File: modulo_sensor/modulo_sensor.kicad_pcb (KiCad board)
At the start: 2 copper layers, 112.4 x 36.6 mm, 33 parts, among them J1 Conn_01x08_Pin, U1 74HC14DR2G

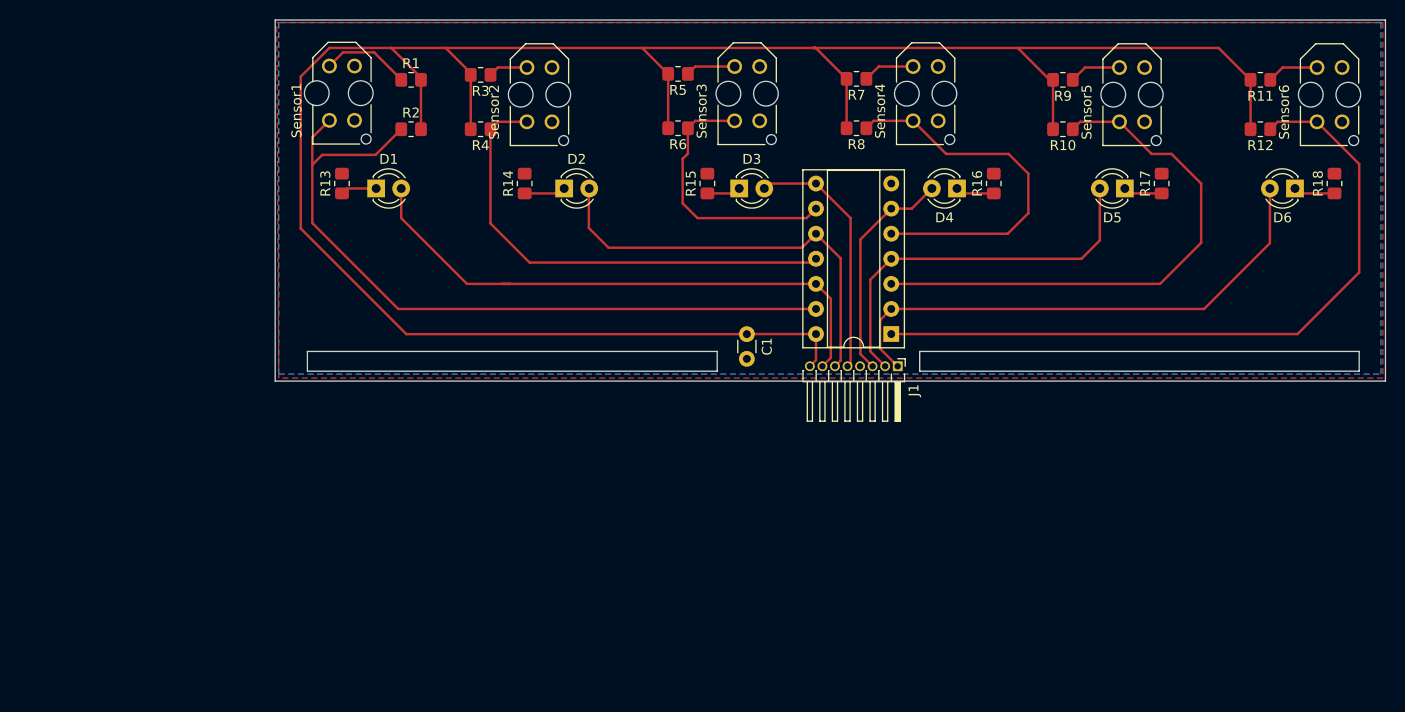
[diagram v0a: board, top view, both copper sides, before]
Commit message: refactor: Pongo el integrado en horizontal
Está todo conectado como antes
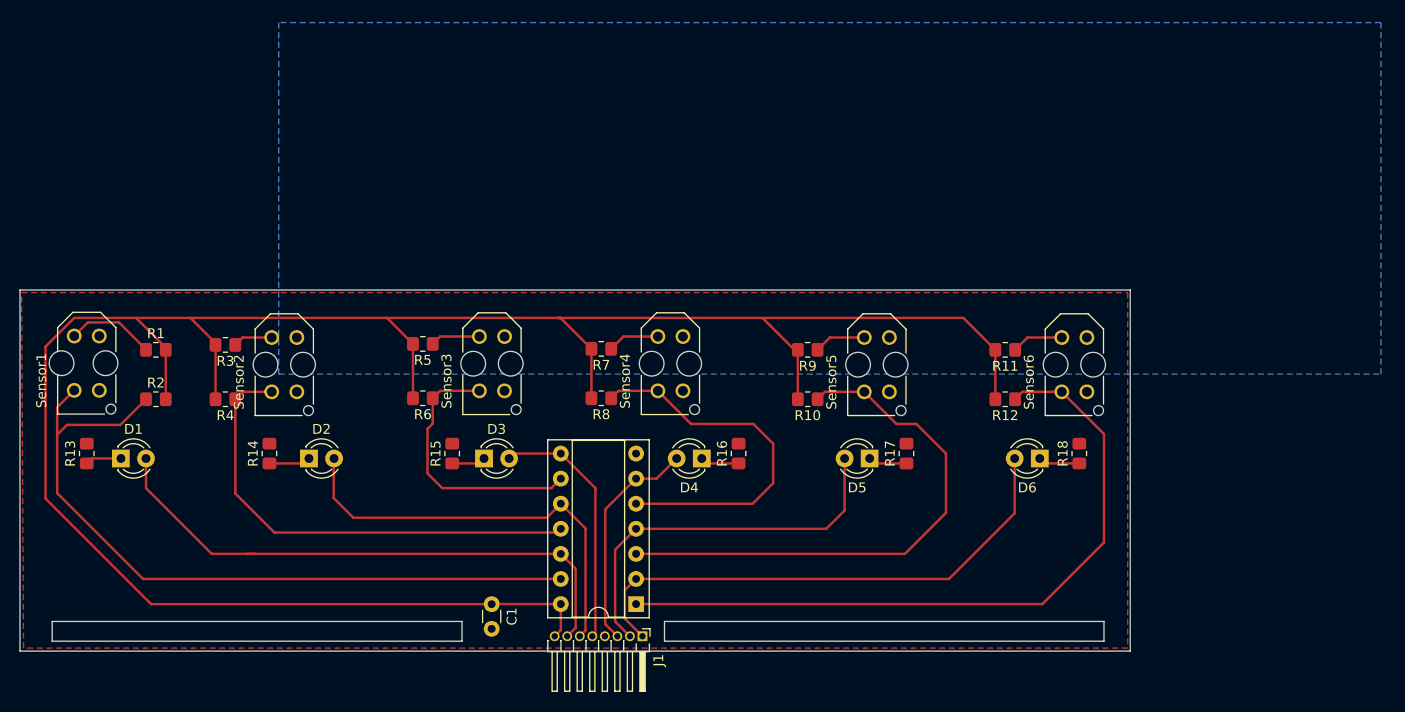
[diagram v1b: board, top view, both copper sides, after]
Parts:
- moved C1 37.6 mm to (90.2, 87.1)
- moved D2 37.6 mm to (71.7, 72.3)
- moved D4 37.6 mm to (111.4, 72.3)
- moved D5 37.6 mm to (128.4, 72.3)
- moved D6 37.6 mm to (145.7, 72.3)
- moved J1 37.6 mm to (105.4, 90.3)
- moved R1 37.6 mm to (56.2, 61.3)
- moved R10 37.6 mm to (122.2, 66.3)
- moved R11 37.6 mm to (142.2, 61.3)
- moved R12 37.6 mm to (142.2, 66.3)
- moved R13 37.6 mm to (49.2, 71.8)
- moved R14 37.6 mm to (67.7, 71.8)
- moved R15 37.6 mm to (86.2, 71.8)
- moved R16 37.6 mm to (115.2, 71.8)
- moved R17 37.6 mm to (132.2, 71.8)
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
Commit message: fix: Guardo el archivo (fallo del commit anterior)
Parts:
- moved U1 13.8 mm to (94.9, 77.4), turned to -90 degrees
- moved D4 5.27 mm to (106.5, 70.5)
- moved R16 4.67 mm to (110.5, 71.5), turned to -90 degrees
- moved C1 2.43 mm to (92.5, 87.8)
- moved D5 2.31 mm to (127.0, 70.5)
- moved R17 2.19 mm to (130.0, 71.5), turned to -90 degrees
- moved D1 1.84 mm to (52.6, 70.5)
- moved D2 1.84 mm to (71.7, 70.5)
- moved D3 1.84 mm to (89.4, 70.5)
- moved D6 1.84 mm to (145.7, 70.5)
- moved J1 1.61 mm to (104.8, 88.8)
- moved R1 0.84 mm to (56.2, 60.5)
- moved R11 0.84 mm to (142.2, 60.5)
- moved R9 0.84 mm to (122.2, 60.5)
- moved R7 0.74 mm to (101.3, 60.5)
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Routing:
- net /Led_Sensor4: track 22.7 -> 52.8 mm
- net /Led_Sensor3: track 25.5 -> 54.6 mm
- net GND: track 0.62 -> 28.0 mm
- net /Led_Sensor5: track 39.5 -> 63.7 mm
- net /Sensor6: track 72.1 -> 57.9 mm
- net /Led_Sensor6: track 53.6 -> 67.7 mm
- net vcc: track 227.2 -> 239.4 mm
- net /Sensor3: track 27.4 -> 37.3 mm
- net /Sensor4: track 37.7 -> 46.7 mm
- net /Led_Sensor2: track 43.2 -> 48.9 mm
- net /Sensor5: track 55.0 -> 59.3 mm
- net /Sensor2: track 48.3 -> 52.3 mm
- net /Led_Sensor1: track 57.9 -> 60.9 mm
- net /Sensor1: track 76.2 -> 73.4 mm
- net Net-(D5-K): track 3.93 -> 2.96 mm
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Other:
- outline, holes or cut-outs redrawn

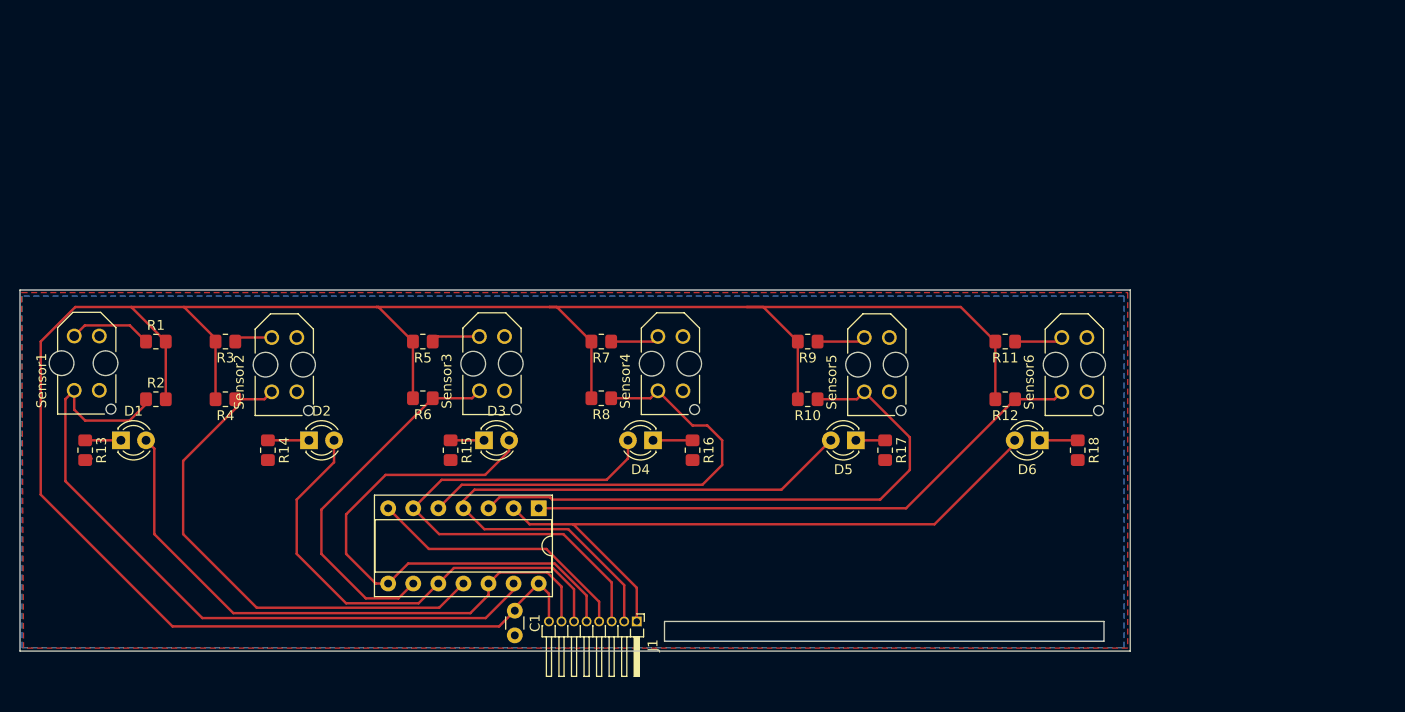
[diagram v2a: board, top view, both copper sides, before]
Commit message: refactor: Los sensores ahora están en la capa de abajo
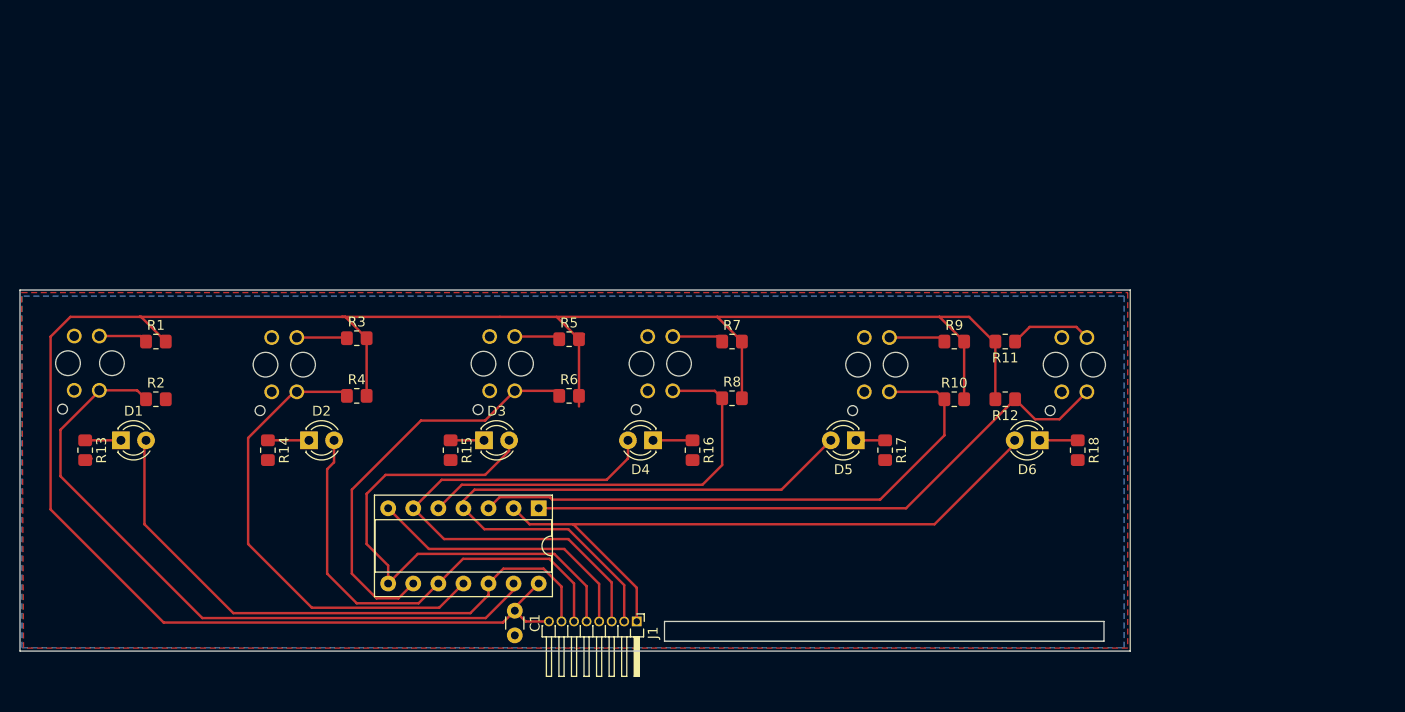
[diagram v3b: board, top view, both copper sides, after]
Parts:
- Sensor1, Sensor2, Sensor3, Sensor4, Sensor5, Sensor6: moved to B.Cu
- moved R10 14.8 mm to (137.0, 66.3), turned to 0 degrees
- moved R9 14.8 mm to (137.0, 60.5), turned to 0 degrees
- moved R5 14.8 mm to (98.0, 60.3), turned to 0 degrees
- moved R6 14.8 mm to (98.0, 66.0), turned to 0 degrees
- moved R3 13.3 mm to (76.5, 60.2), turned to 0 degrees
- moved R4 13.3 mm to (76.5, 66.0), turned to 0 degrees
- moved R7 13.2 mm to (114.5, 60.5), turned to 0 degrees
- moved R8 13.2 mm to (114.5, 66.2), turned to 0 degrees
- moved Sensor3 1.04 mm to (91.2, 62.7)
- moved Sensor4 1.03 mm to (107.2, 62.7)
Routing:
- net vcc: track 239.4 -> 223.7 mm
- net /Sensor3: track 37.3 -> 41.7 mm
- net /Sensor6: track 57.9 -> 62.1 mm
- net /Sensor4: track 46.7 -> 42.6 mm
- net /Sensor2: track 52.3 -> 48.3 mm
- net /Sensor1: track 73.4 -> 69.6 mm
- net Net-(R11-Pad1): track 4.90 -> 8.33 mm
- net Net-(R1-Pad1): track 8.39 -> 4.96 mm
- net GND: track 28.0 -> 30.2 mm
- net /Led_Sensor2: track 48.9 -> 46.8 mm
- net Net-(R3-Pad1): track 3.86 -> 5.10 mm
- net /Led_Sensor3: track 54.6 -> 53.5 mm
- net Net-(R9-Pad1): track 4.90 -> 5.74 mm

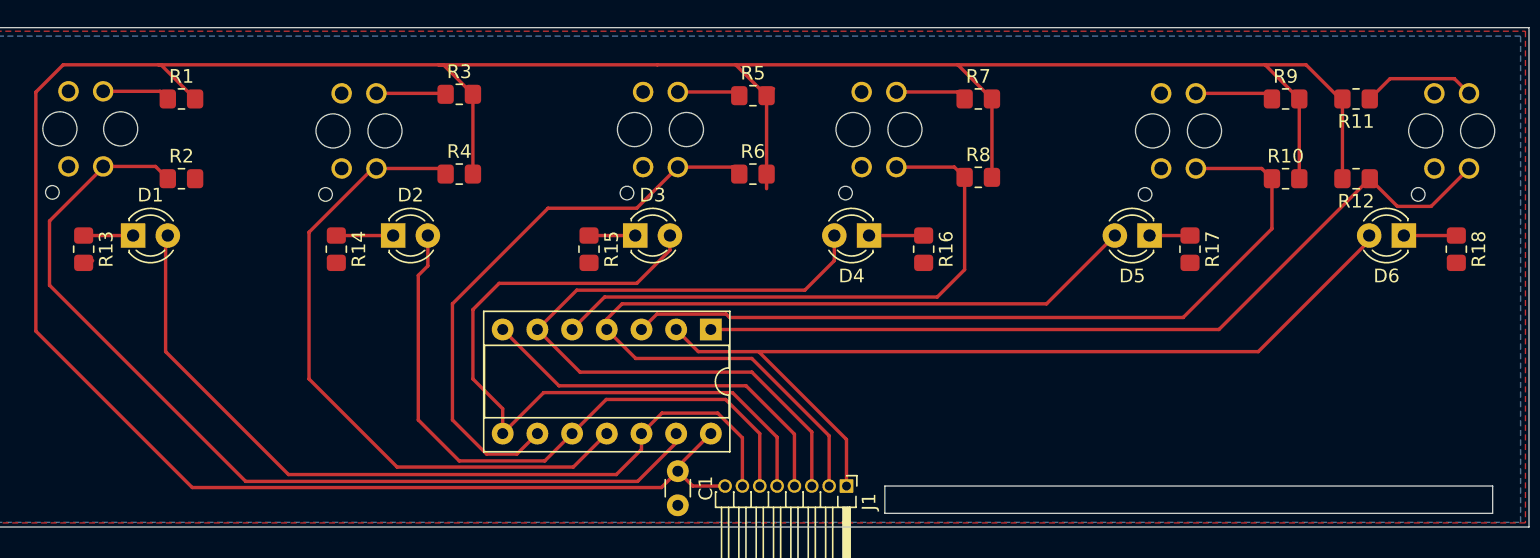
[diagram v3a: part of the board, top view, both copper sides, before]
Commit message: refactor: Cambio las huellas de los led por SMDs
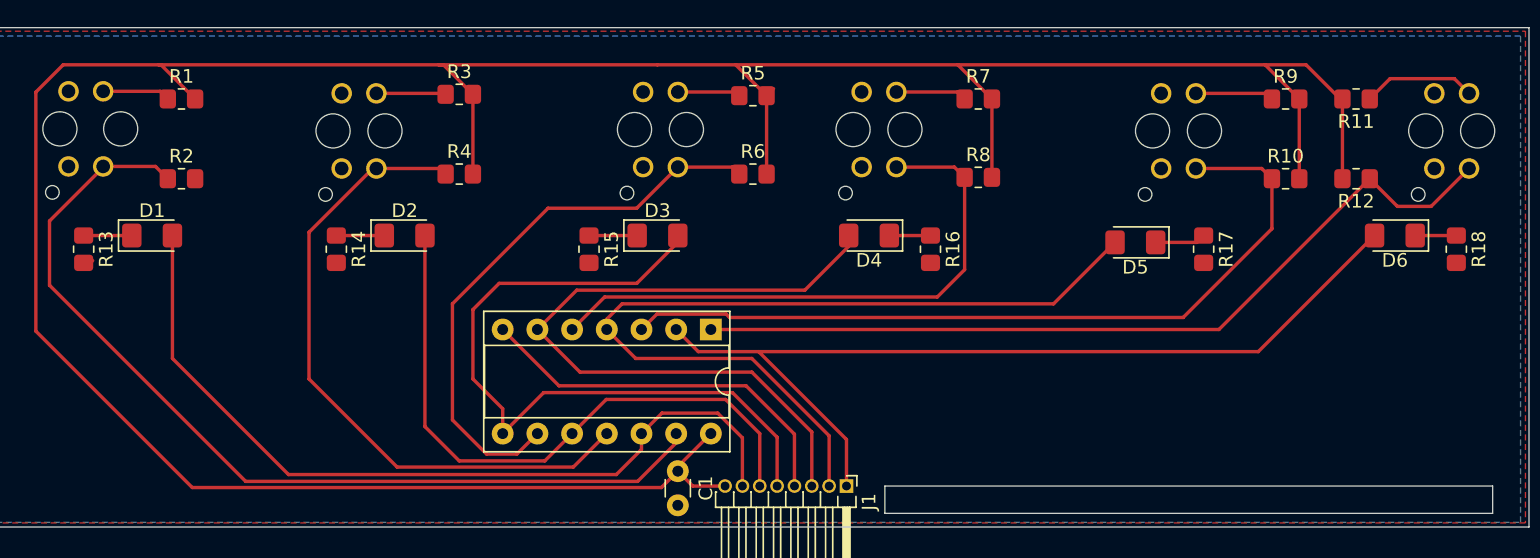
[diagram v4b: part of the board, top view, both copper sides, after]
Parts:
- D1, D2, D3, D4, D5, D6: footprint LED_THT:LED_D3.0mm -> LED_SMD:LED_1206_3216Metric_Pad1.42x1.75mm_HandSolder
- moved D3 1.63 mm to (91.0, 70.5)
- moved D1 1.39 mm to (54.0, 70.5)
- moved D5 1.15 mm to (126.0, 71.0)
- moved R17 1.00 mm to (131.0, 71.5)
- moved D2 0.84 mm to (72.5, 70.5)
- moved D6 0.66 mm to (145.0, 70.5)
- moved R16 0.50 mm to (111.0, 71.5)
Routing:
- net vcc: track 223.7 -> 222.6 mm
- net Net-(D4-K): track 4.00 -> 3.01 mm
- net Net-(D6-K): track 3.84 -> 3.01 mm
- net Net-(D5-K): track 2.96 -> 3.72 mm
- net Net-(D2-K): track 4.16 -> 3.51 mm

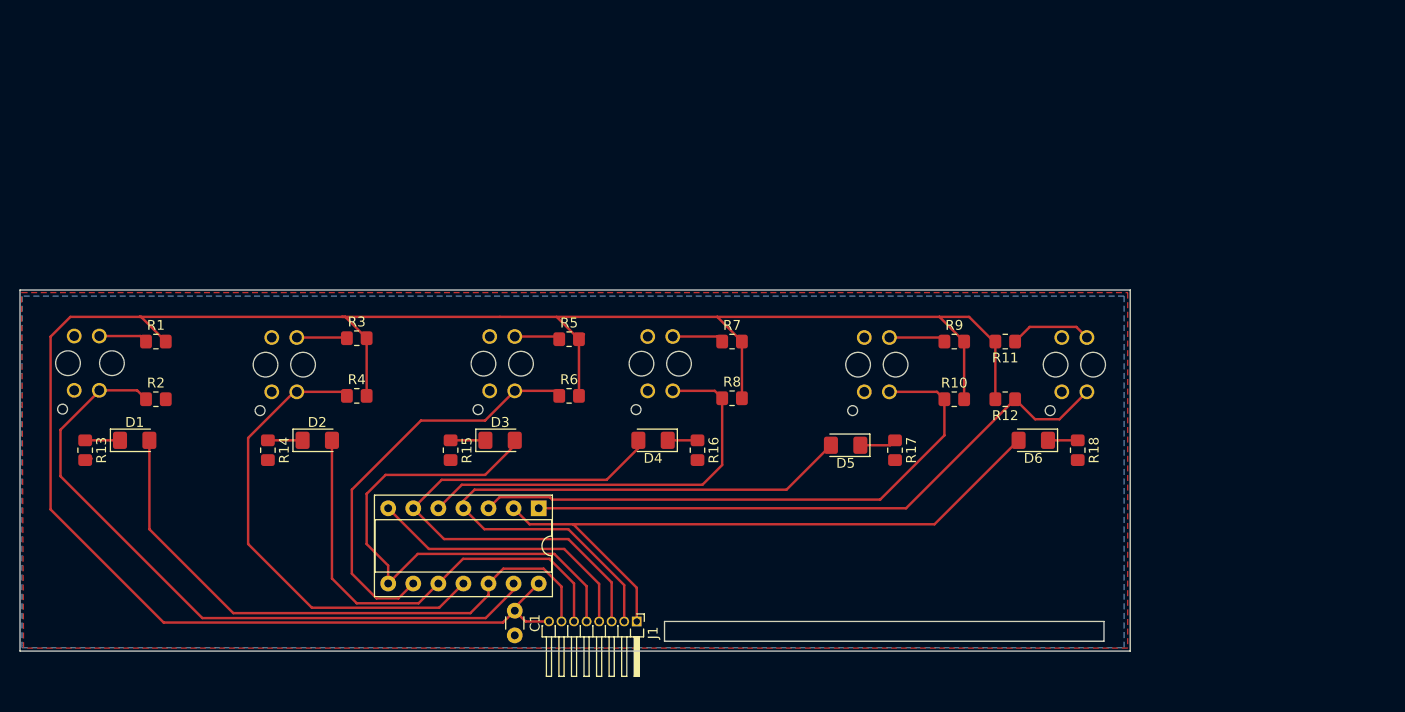
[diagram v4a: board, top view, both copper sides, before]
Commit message: feat: Reestructuro la placa a doble faz y pasa el DRC sin errores
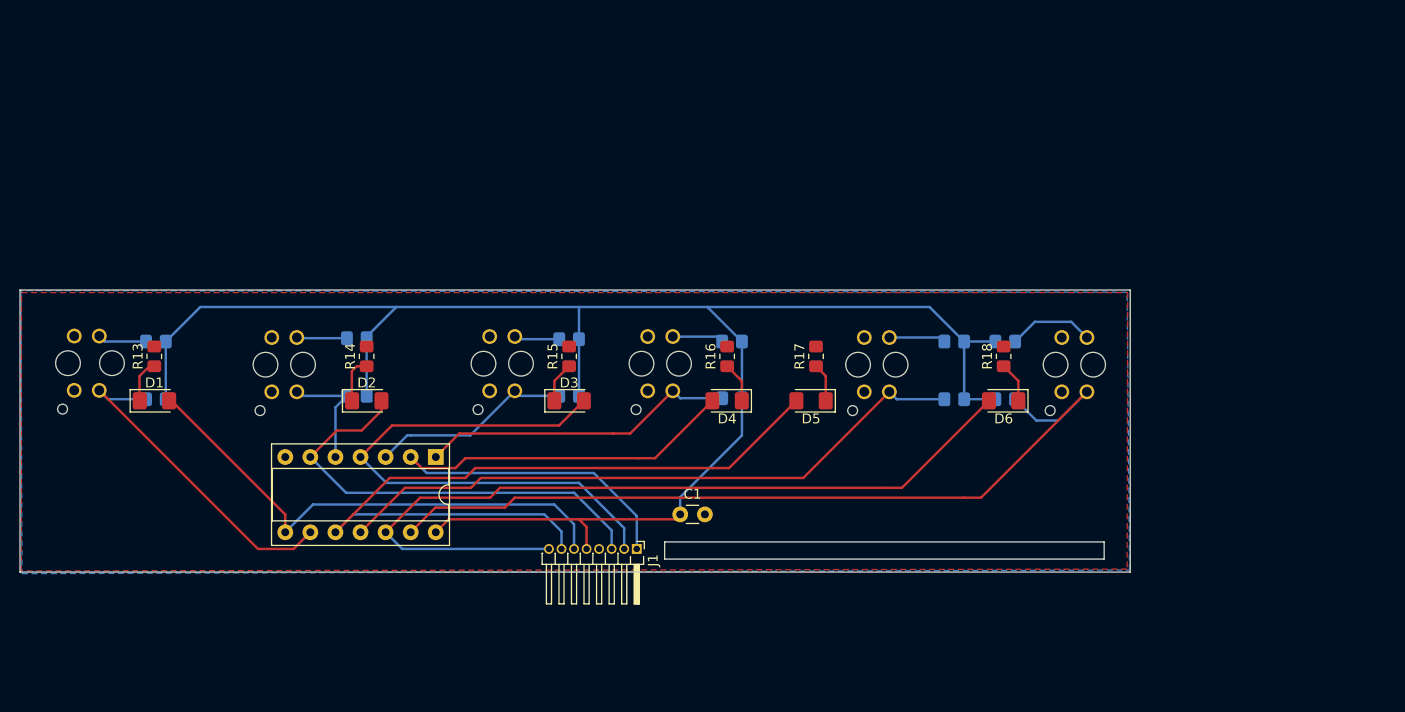
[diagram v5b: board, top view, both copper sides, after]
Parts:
- R1, R10, R11, R12, R2, R3, R4, R5, R6, R7, R8, R9: moved to B.Cu
- moved C1 19.4 mm to (109.2, 78.0), turned to 0 degrees
- moved R15 15.3 mm to (98.0, 62.0), turned to 90 degrees
- moved R14 13.8 mm to (77.5, 62.0), turned to 90 degrees
- moved R17 12.4 mm to (123.0, 62.0), turned to 90 degrees
- moved R18 12.1 mm to (142.0, 62.0), turned to 90 degrees
- moved R13 11.8 mm to (56.0, 62.0), turned to 90 degrees
- moved U1 11.6 mm to (84.5, 72.2)
- moved R16 9.96 mm to (114.0, 62.0), turned to 90 degrees
- moved D4 8.50 mm to (114.0, 66.5)
- moved D3 8.05 mm to (98.0, 66.5)
- moved J1 7.34 mm to (104.8, 81.5)
- moved D2 6.41 mm to (77.5, 66.5)
- moved D5 5.70 mm to (122.5, 66.5)
- moved D6 5.00 mm to (142.0, 66.5)
- moved D1 4.47 mm to (56.0, 66.5)
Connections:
- J1 pad 1: /Led_Sensor6 -> /Led_Sensor4
- J1 pad 2: /Led_Sensor5 -> /Led_Sensor3
- J1 pad 3: /Led_Sensor4 -> /Led_Sensor2
- J1 pad 5: /Led_Sensor3 -> vcc
- J1 pad 6: /Led_Sensor2 -> /Led_Sensor1
- J1 pad 7: /Led_Sensor1 -> /Led_Sensor5
- J1 pad 8: vcc -> /Led_Sensor6
- U1 pad 1: /Sensor6 -> /Sensor4
- U1 pad 10: /Led_Sensor2 -> /Led_Sensor5
- U1 pad 11: /Sensor2 -> /Sensor5
- U1 pad 12: /Led_Sensor1 -> /Led_Sensor6
- U1 pad 13: /Sensor1 -> /Sensor6
- U1 pad 2: /Led_Sensor6 -> /Led_Sensor4
- U1 pad 3: /Sensor5 -> /Sensor3
- U1 pad 4: /Led_Sensor5 -> /Led_Sensor3
- U1 pad 5: /Sensor4 -> /Sensor2
- U1 pad 6: /Led_Sensor4 -> /Led_Sensor2
- U1 pad 8: /Led_Sensor3 -> /Led_Sensor1
- U1 pad 9: /Sensor3 -> /Sensor1
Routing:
- net vcc: track 222.6 -> 176.9 mm
- net /Sensor2: track 48.3 -> 12.1 mm
- net /Sensor1: track 69.6 -> 33.8 mm
- net GND: track 30.2 -> 0.00 mm
- net /Sensor6: track 62.1 -> 83.8 mm
- net /Sensor3: track 41.7 -> 20.6 mm
- net /Led_Sensor6: track 67.7 -> 83.9 mm
- net /Led_Sensor5: track 63.5 -> 78.3 mm
- net /Sensor4: track 42.6 -> 32.1 mm
- net /Led_Sensor4: track 53.3 -> 62.6 mm
- net /Led_Sensor1: track 61.1 -> 52.1 mm
- net /Sensor5: track 59.0 -> 65.3 mm
- net /Led_Sensor3: track 53.2 -> 56.8 mm
- net Net-(D2-K): track 3.51 -> 4.72 mm
- net Net-(D6-K): track 3.01 -> 4.12 mm
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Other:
- board size 112.4 x 36.6 mm -> 112.4 x 28.6 mm
- board text added: "Anterior medida"
